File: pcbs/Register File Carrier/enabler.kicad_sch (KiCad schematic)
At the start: 3 parts, among them U3001 74HC14, U3002 74HC08, U3003 74HC138

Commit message: Adding some more bits
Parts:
- added U3004: 74HC08, Package_SO:SOIC-14_3.9x8.7mm_P1.27mm, symbol 74xx:74LS08
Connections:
- net +5V: now also U3003.16 (VCC)
- net Cycle3: now also U3004.10
- net GND: now also U3001.9, U3003.8 (GND), U3004.1, U3004.2; no longer U3001.3
- net ~{Enable}: now also U3003.4 (~{E0})
- net at U3001.8: no longer U3002.4
- net at U3002.3: now also U3002.4; no longer U3001.9
- net I0: now reaches U3003.1 (A0)
- net ~{BranchZero}: now reaches U3003.10 (~{Y5})
- net ~{BranchZero}: now also U3004.9
- net ~{LoadPC}: now reaches U3003.11 (~{Y4})
- net ~{StoreW}: now reaches U3003.12 (~{Y3})
- net ~{StoreW}: now also U3004.12
- net ~{StoreB}: now reaches U3003.13 (~{Y2})
- net ~{StoreB}: now also U3004.13
- net ~{LoadW}: now reaches U3003.14 (~{Y1})
- net ~{LoadB}: now reaches U3003.15 (~{Y0})
- net I1: now reaches U3003.2 (A1)
- net I2: now reaches U3003.3 (A2)
- net I3: now reaches U3003.6 (E2)
- net ~{Set}: now reaches U3003.7 (~{Y7})
- net ~{Set}: now also U3001.3
- net ~{Halt}: now reaches U3003.9 (~{Y6})
- net ~{AB_{Enable}}: now reaches U3001.4
- new net: U3004.4, U3004.8
- new net: U3004.11, U3004.5
- new net RegCLK: U3004.6
- no-connect marks 3 -> 4
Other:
- moved on the sheet: U3001A, U3001B, U3001D, U3002B, U3002C, U3002D

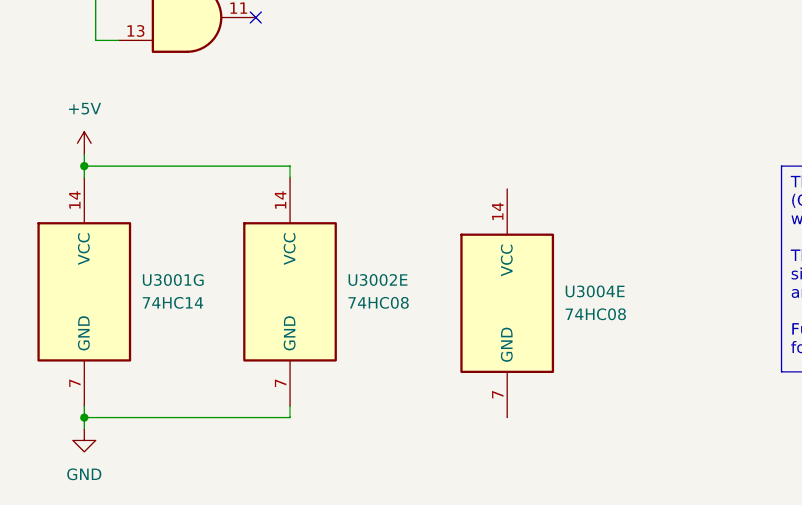
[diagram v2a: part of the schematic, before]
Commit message: Setting up some LEDs
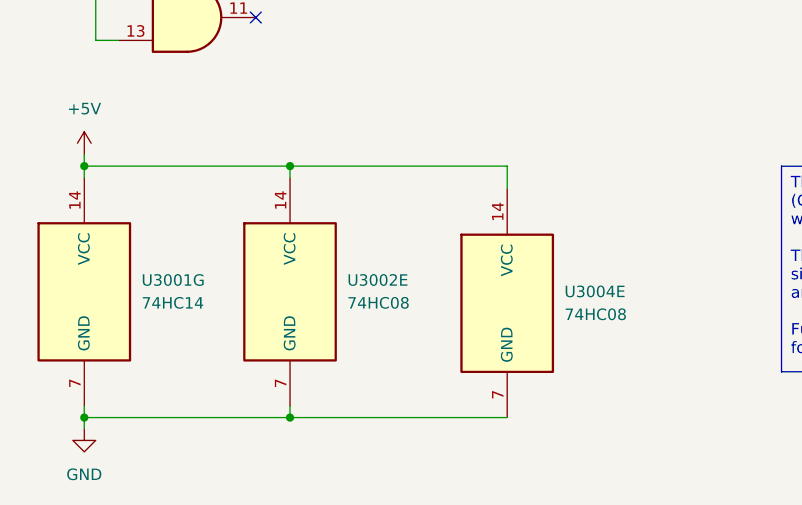
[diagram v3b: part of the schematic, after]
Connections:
- net +5V: now also U3004.14 (VCC)
- net GND: now also U3004.7 (GND)
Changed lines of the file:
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@@
+	)
+	(junction
+		(at 44.45 160.02)
+		(diameter 0)
+		(color 0 0 0 0)
 	)
 	(junction
 		(at 22.86 111.76)
+		(diameter 0)
+		(color 0 0 0 0)
+	)
+	(junction
+		(at 44.45 187.96)
 		(diameter 0)
 		(color 0 0 0 0)
@@
 	(wire
 		(pts
+			(xy 44.45 187.96) (xy 68.58 187.96)
+		)
+		(stroke
+			(width 0)
+			(type default)
+		)
+	)
+	(wire
+		(pts
 			(xy 130.81 134.62) (xy 142.24 134.62)
 		)
@@
 		)
 	)
+	(wire
+		(pts
+			(xy 44.45 160.02) (xy 68.58 160.02)
+		)
+		(stroke
+			(width 0)
+			(type default)
+		)
+	)
 	(bus
 		(pts
@@
 		)
 		(stroke
+			(width 0)
+			(type default)
+		)
+	)
+	(wire
+		(pts
+			(xy 68.58 160.02) (xy 68.58 162.56)
+		)
+		(stroke

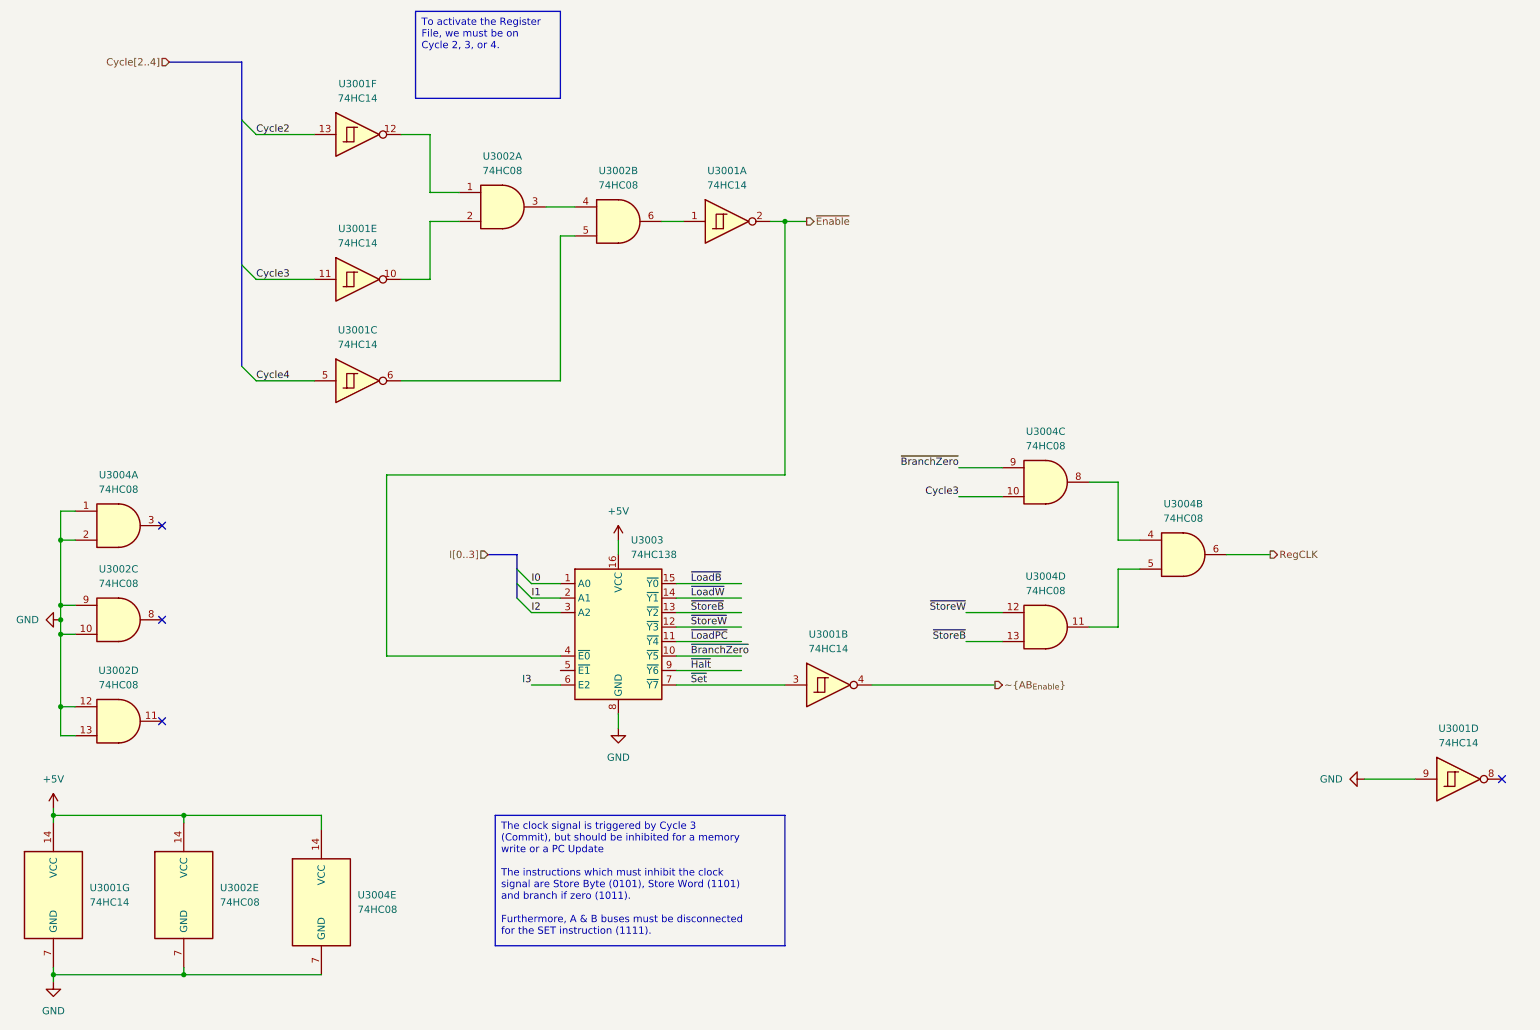
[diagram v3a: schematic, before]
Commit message: More LEDs and routing
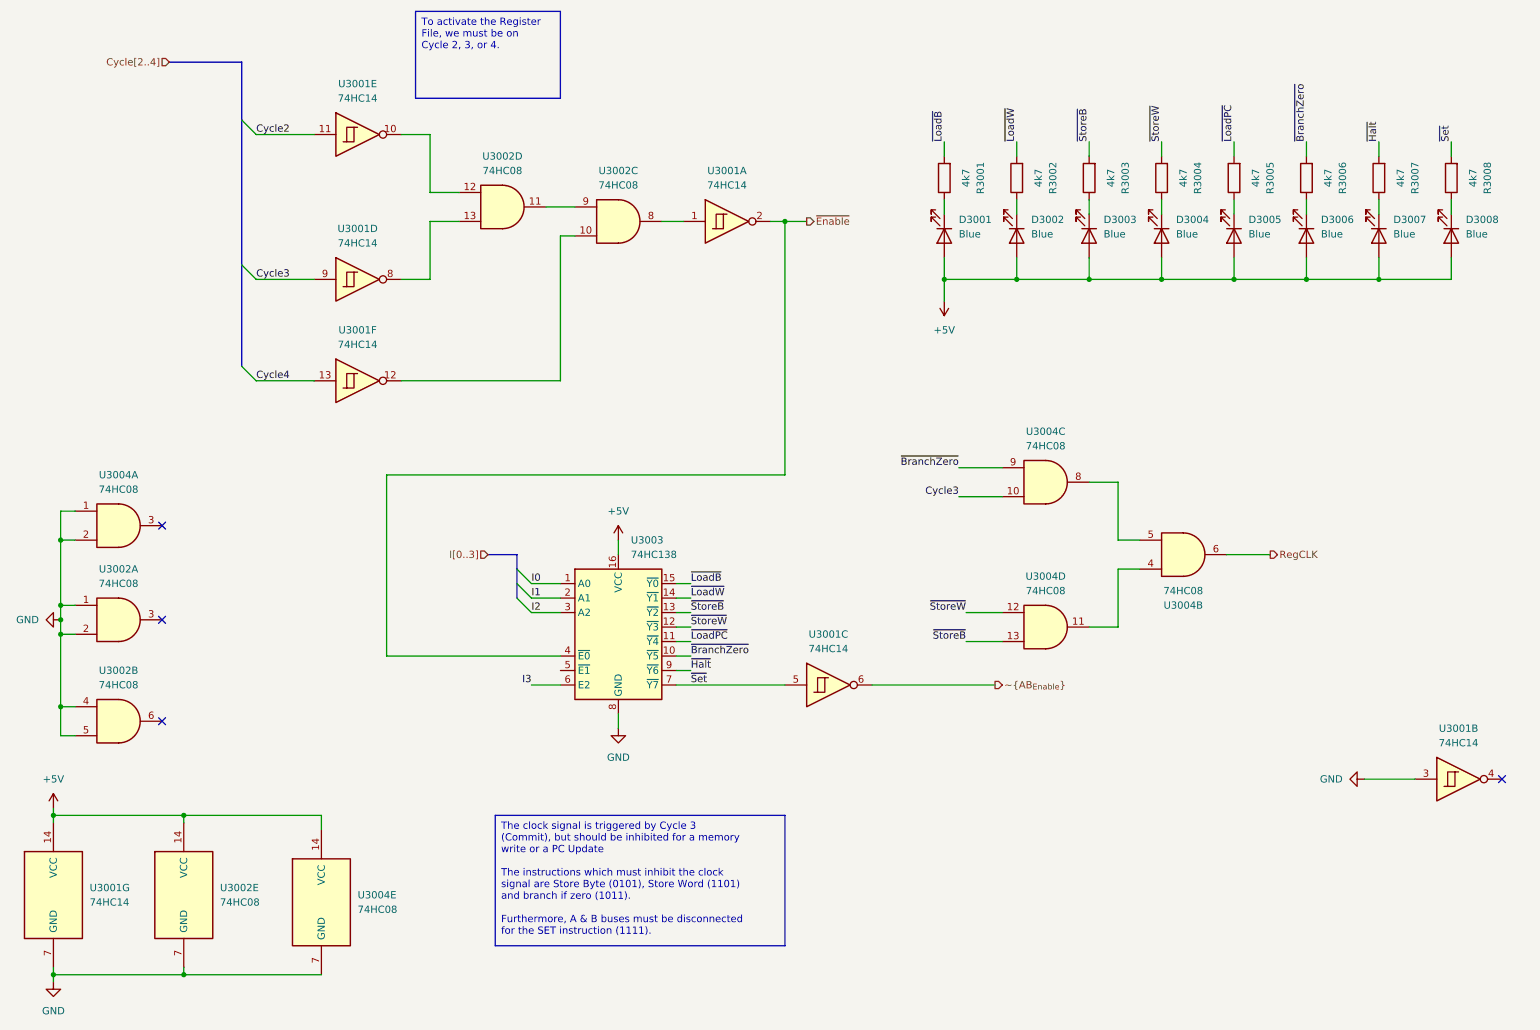
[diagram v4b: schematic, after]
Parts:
- added D3001, D3002, D3003, D3004, D3005, D3006, D3007, D3008: Blue, LED_SMD:LED_0603_1608Metric, symbol Device:LED
- added R3001, R3002, R3003, R3004, R3005, R3006, R3007, R3008: 4k7, Resistor_SMD:R_0603_1608Metric, symbol Device:R
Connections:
- net +5V: now also D3001.2 (A), D3002.2 (A), D3003.2 (A), D3004.2 (A), D3005.2 (A), D3006.2 (A), D3007.2 (A), D3008.2 (A)
- net Cycle2: now also U3001.11; no longer U3001.13
- net Cycle3: now also U3001.9; no longer U3001.11
- net Cycle4: now also U3001.13; no longer U3001.5
- net GND: now also U3001.3, U3002.1, U3002.2, U3002.4, U3002.5; no longer U3001.9, U3002.10, U3002.12, U3002.13, U3002.9
- net ~{AB_{Enable}}: now also U3001.6; no longer U3001.4
- net ~{BranchZero}: now also R3006.2
- net ~{Halt}: now also R3007.2
- net ~{LoadB}: now also R3001.2
- net ~{LoadPC}: now also R3005.2
- net ~{LoadW}: now also R3002.2
- net ~{Set}: now also U3001.5, R3008.2; no longer U3001.3
- net ~{StoreB}: now also R3003.2
- net ~{StoreW}: now also R3004.2
- net at U3004.8: now also U3004.5; no longer U3004.4
- net at U3001.8: now also U3002.13
- net at U3001.1: now also U3002.8; no longer U3002.6
- net at U3001.12: now also U3002.10; no longer U3002.1
- net at U3001.10: now also U3002.12; no longer U3002.2
- net at U3002.3: no longer U3002.4
- net at U3004.11: now also U3004.4; no longer U3004.5
- net at U3002.11: now also U3002.9
- new net: D3008.1 (K), R3008.1
- new net: D3002.1 (K), R3002.1
- new net: D3003.1 (K), R3003.1
- new net: D3005.1 (K), R3005.1
- new net: D3007.1 (K), R3007.1
- new net: D3001.1 (K), R3001.1
- new net: D3004.1 (K), R3004.1
- new net: D3006.1 (K), R3006.1
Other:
- moved on the sheet: U3001B, U3001C, U3001D, U3001E, U3001F, U3002A, U3002B, U3002C, U3002D

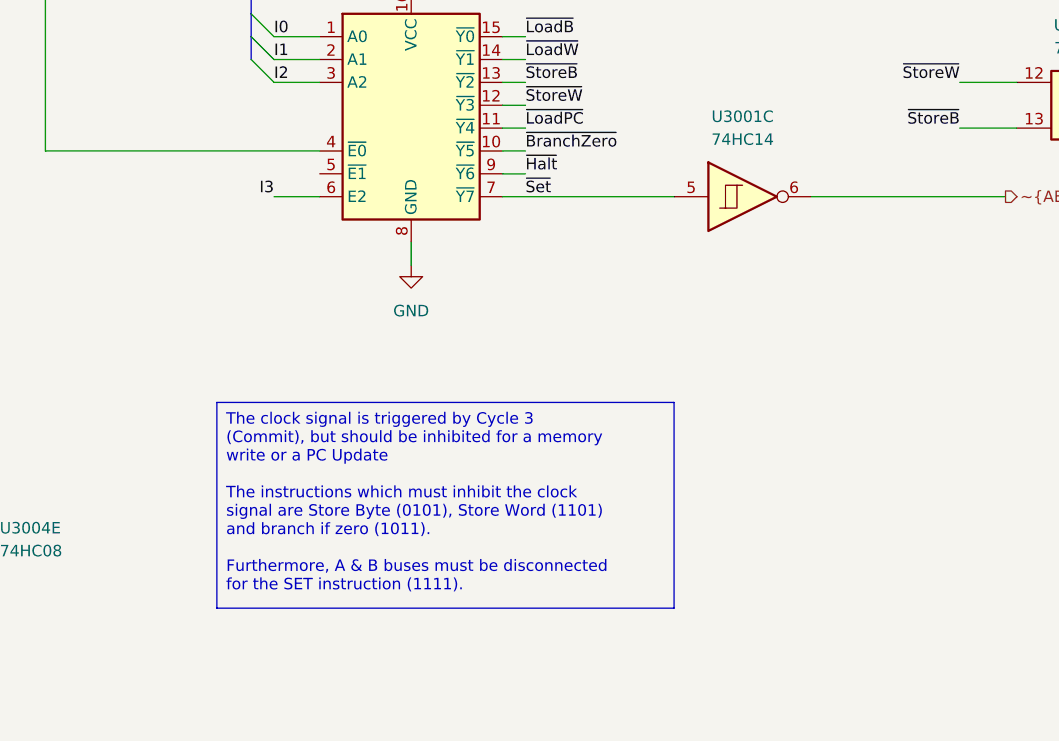
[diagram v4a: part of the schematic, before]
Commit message: Shrink board slightly
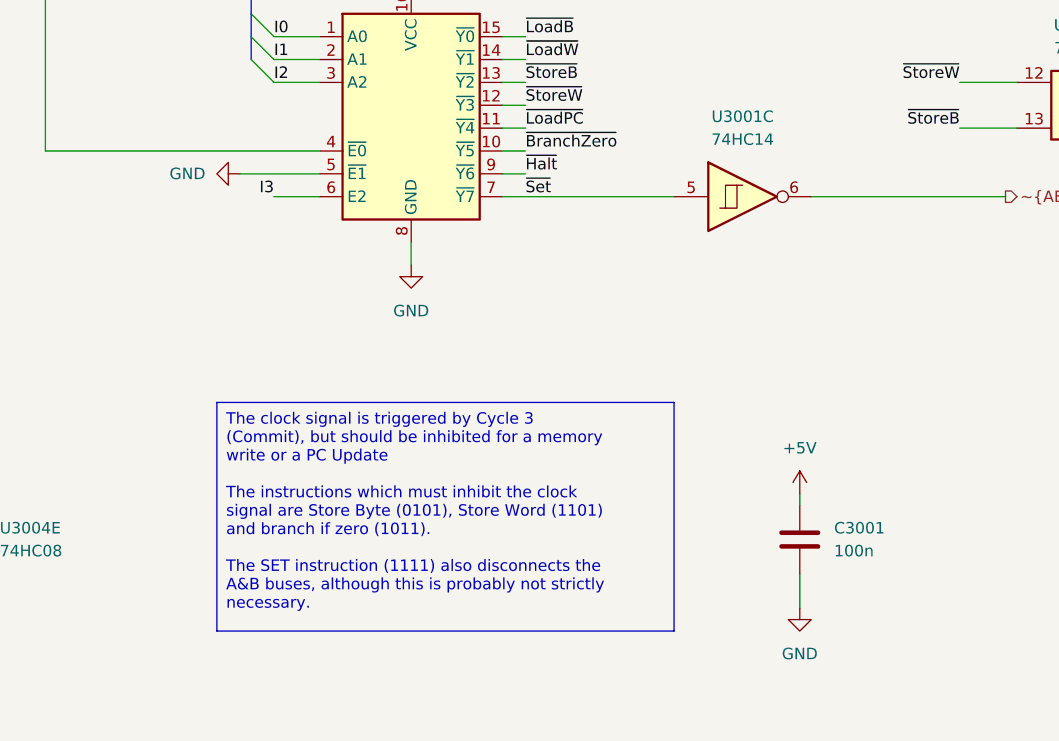
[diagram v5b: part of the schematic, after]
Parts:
- added C3001: 100n, Capacitor_SMD:C_0603_1608Metric, symbol Device:C
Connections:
- net +5V: now also C3001.1
- net GND: now also U3003.5 (~{E1}), C3001.2

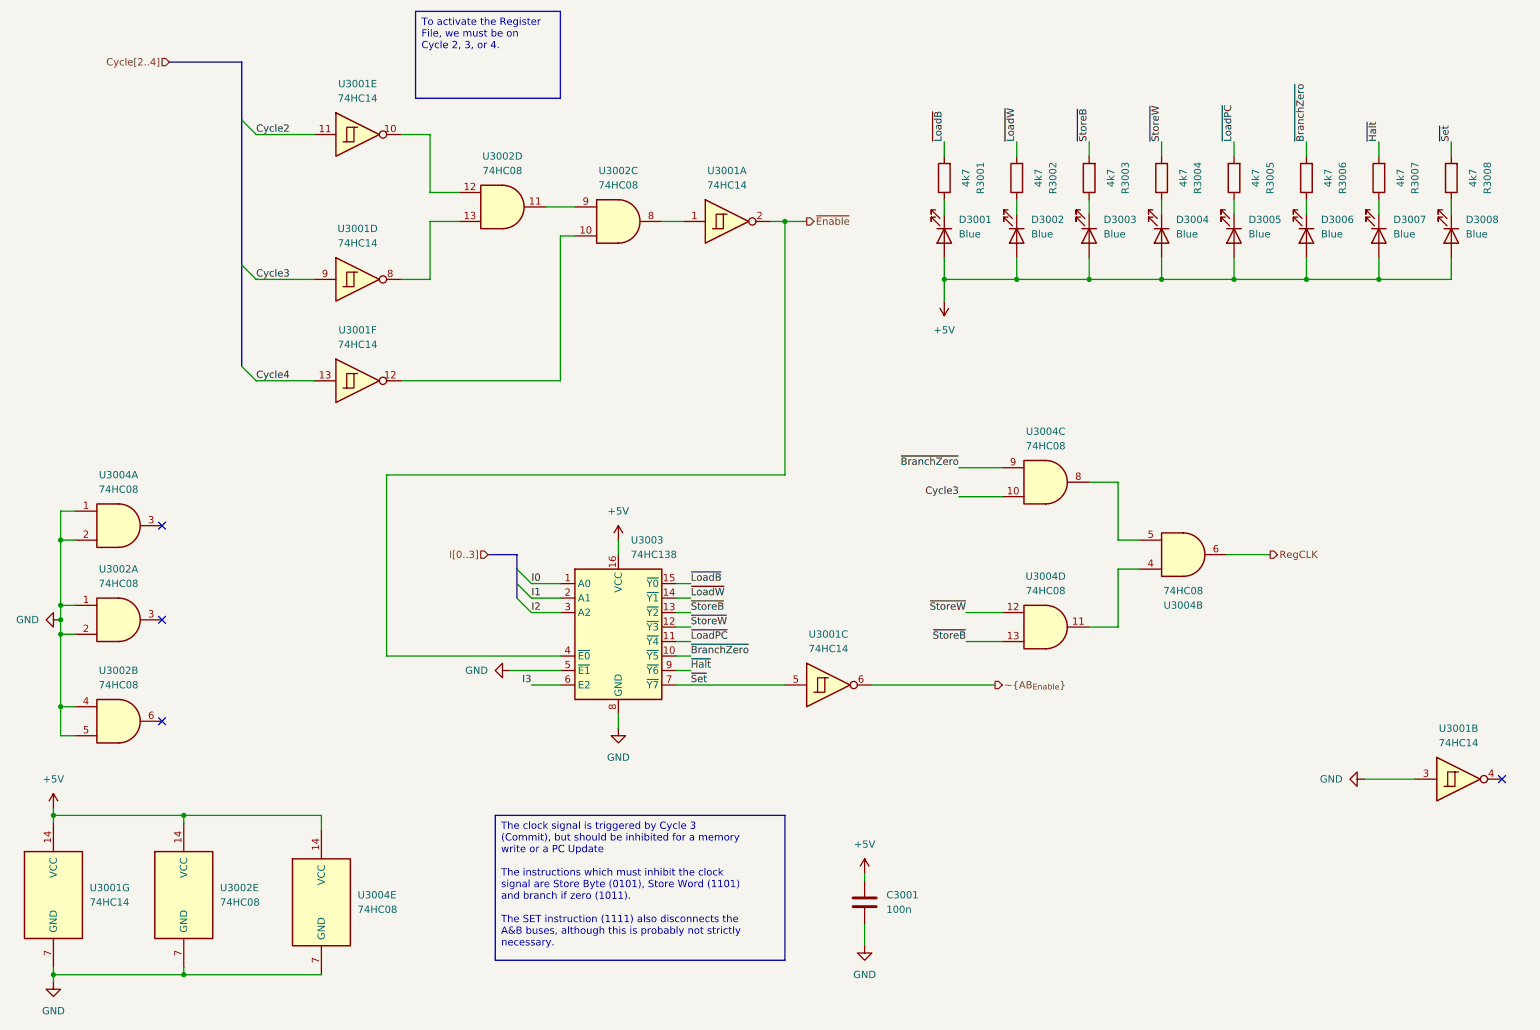
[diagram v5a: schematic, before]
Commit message: Output buffers were a bad idea which were about to cause trouble
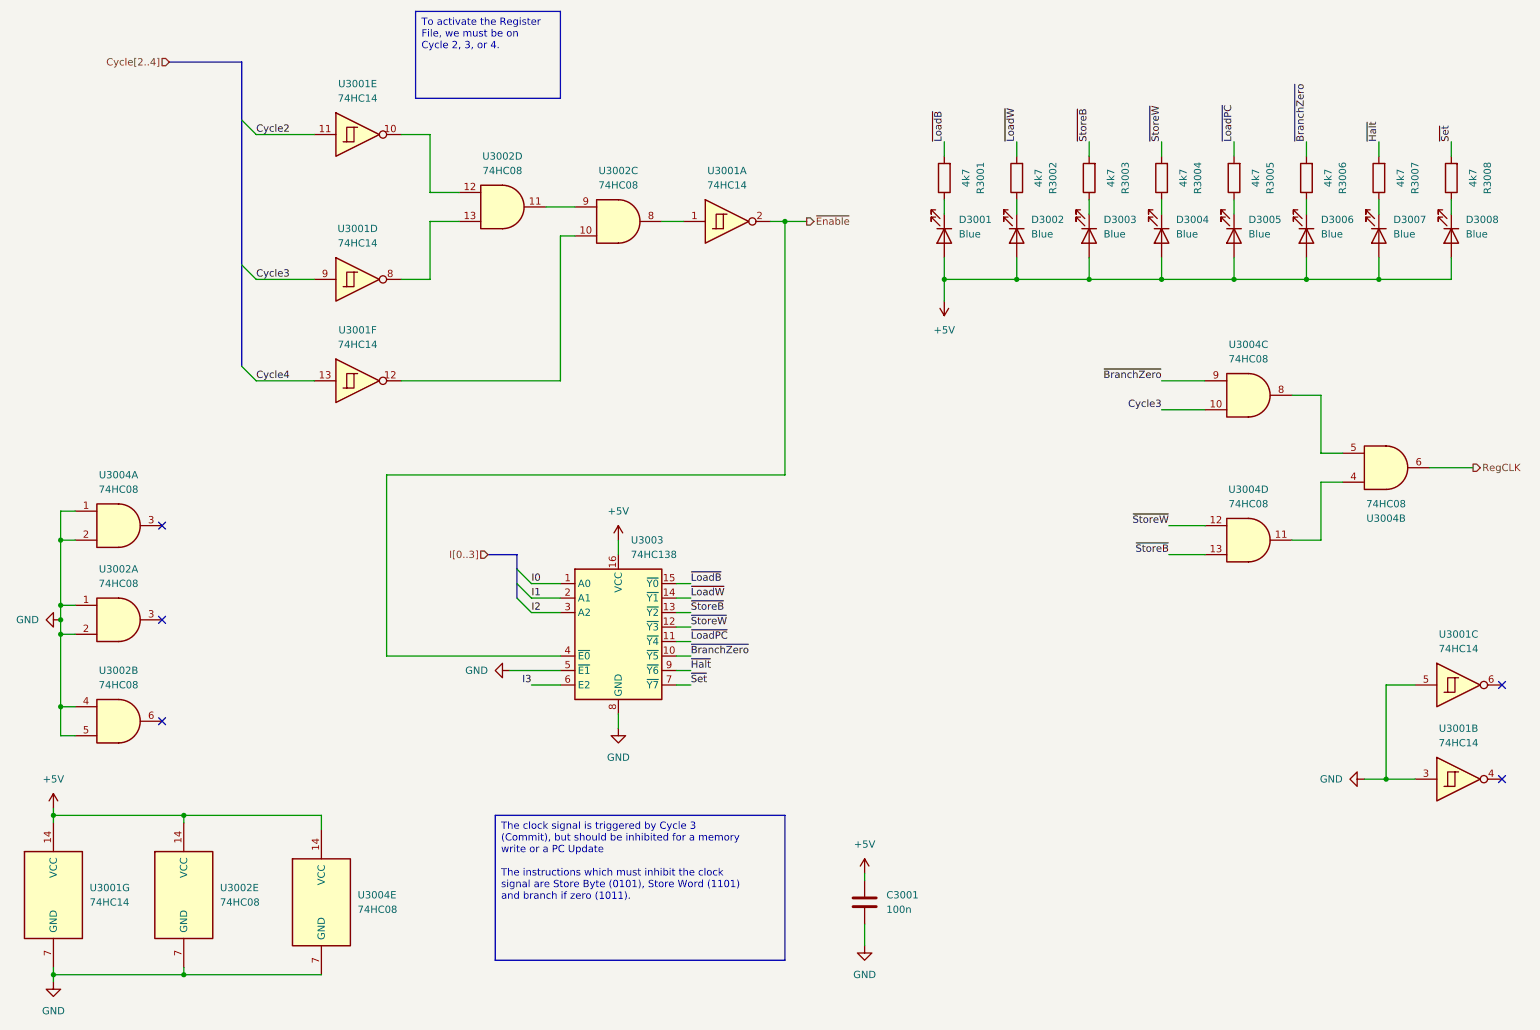
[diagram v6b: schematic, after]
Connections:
- net GND: now also U3001.5
- net ~{Set}: no longer U3001.5
- net ~{AB_{Enable}}: no longer names the net of U3001.6
- no-connect marks 4 -> 5
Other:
- moved on the sheet: U3004B, U3004C, U3004D

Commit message: Add Active indicator
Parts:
- added D3009: Blue, LED_SMD:LED_0603_1608Metric, symbol Device:LED
- added R3009: 4k7, Resistor_SMD:R_0603_1608Metric, symbol Device:R
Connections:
- net +5V: now also D3009.2 (A)
- net ~{Enable}: now also R3009.1
- new net: D3009.1 (K), R3009.2
